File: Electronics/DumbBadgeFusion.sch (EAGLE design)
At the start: 103 parts, among them IC1 SN74CBT16233DGGR, IC2 SN74CBT16233DGGR, SW1 SPST_TACT-KMR2, U1 TDP3E001DRLR-SOT-23-5SOT-23-5, U6 MAX3232, U7 TPS61090RSAR, U8 MCP73831T-2ACI/OT, X4 32.768

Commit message: beginning Firmware
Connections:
- new net LCD0: U$4.PB00
- new net LCD1: U$4.PB01
- new net LCD10: U$4.PB10
- new net LCD11: U$4.PB11
- new net LCD12: U$4.PB12
- new net LCD13: U$4.PB13
- new net LCD14: U$4.PB14
- new net LCD15: U$4.PB15
- new net LCD2: U$4.PB02
- new net LCD3: U$4.PB03
- new net LCD4: U$4.PB04
- new net LCD5: U$4.PB05
- new net LCD6: U$4.PB06
- new net LCD7: U$4.PB07
- new net LCD8: U$4.PB08
- new net LCD9: U$4.PB09
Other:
- moved on the sheet: U$4
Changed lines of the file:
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@@
 <attribute name="SHEET" x="363.22" y="-0.635" size="2.54" layer="94" font="vector"/>
 </instance>
-<instance part="U$4" gate="G$1" x="152.4" y="78.74" smashed="yes">
-<attribute name="NAME" x="137.16" y="12.7" size="1.778" layer="95"/>
-<attribute name="VALUE" x="137.16" y="104.648" size="1.778" layer="96"/>
+<instance part="U$4" gate="G$1" x="175.26" y="81.28" smashed="yes">
+<attribute name="NAME" x="160.02" y="15.24" size="1.778" layer="95"/>
+<attribute name="VALUE" x="160.02" y="107.188" size="1.778" layer="96"/>
 </instance>
 <instance part="IC1" gate="G$1" x="248.92" y="226.06" smashed="yes">
@@
 </instances>
 <busses>
+<bus name="LCD[0..15]">
+<segment>
+<wire x1="134.62" y1="81.28" x2="134.62" y2="43.18" width="0.762" layer="92"/>
+<label x="133.35" y="58.928" size="1.778" layer="95" rot="R90"/>
+</segment>
+</bus>
 </busses>
 <nets>
@@
 </segment>
 </net>
+<net name="LCD0" class="0">
+<segment>
+<wire x1="134.62" y1="81.28" x2="142.24" y2="81.28" width="0.1524" layer="91"/>
+<wire x1="142.24" y1="81.28" x2="154.94" y2="81.28" width="0.1524" layer="91"/>
+<label x="144.78" y="81.28" size="1.778" layer="95"/>
+<pinref part="U$4" gate="G$1" pin="PB00"/>
+</segment>
+</net>
+<net name="LCD1" class="0">
+<segment>
+<wire x1="134.62" y1="78.74" x2="142.24" y2="78.74" width="0.1524" layer="91"/>
+<wire x1="142.24" y1="78.74" x2="154.94" y2="78.74" width="0.1524" layer="91"/>
+<label x="144.78" y="78.74" size="1.778" layer="95"/>
+<pinref part="U$4" gate="G$1" pin="PB01"/>
+</segment>
+</net>
+<net name="LCD2" class="0">
+<segment>
+<wire x1="134.62" y1="76.2" x2="142.24" y2="76.2" width="0.1524" layer="91"/>
+<wire x1="142.24" y1="76.2" x2="154.94" y2="76.2" width="0.1524" layer="91"/>
+<label x="144.78" y="76.2" size="1.778" layer="95"/>
+<pinref part="U$4" gate="G$1" pin="PB02"/>
+</segment>
+</net>
+<net name="LCD3" class="0">
+<segment>
+<wire x1="134.62" y1="73.66" x2="142.24" y2="73.66" width="0.1524" layer="91"/>
+<wire x1="142.24" y1="73.66" x2="154.94" y2="73.66" width="0.1524" layer="91"/>
+<label x="144.78" y="73.66" size="1.778" layer="95"/>
+<pinref part="U$4" gate="G$1" pin="PB03"/>
+</segment>
+</net>
+<net name="LCD4" class="0">
+<segment>
+<wire x1="134.62" y1="71.12" x2="142.24" y2="71.12" width="0.1524" layer="91"/>
+<wire x1="142.24" y1="71.12" x2="154.94" y2="71.12" width="0.1524" layer="91"/>
+<label x="144.78" y="71.12" size="1.778" layer="95"/>
+<pinref part="U$4" gate="G$1" pin="PB04"/>
+</segment>
+</net>
+<net name="LCD5" class="0">
+<segment>
+<wire x1="134.62" y1="68.58" x2="142.24" y2="68.58" width="0.1524" layer="91"/>
+<wire x1="142.24" y1="68.58" x2="154.94" y2="68.58" width="0.1524" layer="91"/>
+<label x="144.78" y="68.58" size="1.778" layer="95"/>
+<pinref part="U$4" gate="G$1" pin="PB05"/>
+</segment>
+</net>
+<net name="LCD6" class="0">
+<segment>
+<wire x1="134.62" y1="66.04" x2="142.24" y2="66.04" width="0.1524" layer="91"/>
+<wire x1="142.24" y1="66.04" x2="154.94" y2="66.04" width="0.1524" layer="91"/>
+<label x="144.78" y="66.04" size="1.778" layer="95"/>
+<pinref part="U$4" gate="G$1" pin="PB06"/>
+</segment>
+</net>
+<net name="LCD7" class="0">
+<segment>
+<wire x1="134.62" y1="63.5" x2="142.24" y2="63.5" width="0.1524" layer="91"/>
+<wire x1="142.24" y1="63.5" x2="154.94" y2="63.5" width="0.1524" layer="91"/>
+<label x="144.78" y="63.5" size="1.778" layer="95"/>
+<pinref part="U$4" gate="G$1" pin="PB07"/>
+</segment>
+</net>
+<net name="LCD8" class="0">
+<segment>
+<wire x1="134.62" y1="60.96" x2="142.24" y2="60.96" width="0.1524" layer="91"/>
+<wire x1="142.24" y1="60.96" x2="154.94" y2="60.96" width="0.1524" layer="91"/>
+<label x="144.78" y="60.96" size="1.778" layer="95"/>
+<pinref part="U$4" gate="G$1" pin="PB08"/>
+</segment>
+</net>
+<net name="LCD9" class="0">
+<segment>
+<wire x1="134.62" y1="58.42" x2="142.24" y2="58.42" width="0.1524" layer="91"/>
+<wire x1="142.24" y1="58.42" x2="154.94" y2="58.42" width="0.1524" layer="91"/>
+<label x="144.78" y="58.42" size="1.778" layer="95"/>
+<pinref part="U$4" gate="G$1" pin="PB09"/>
+</segment>
+</net>
+<net name="LCD10" class="0">
+<segment>
+<wire x1="134.62" y1="55.88" x2="142.24" y2="55.88" width="0.1524" layer="91"/>
+<wire x1="142.24" y1="55.88" x2="154.94" y2="55.88" width="0.1524" layer="91"/>
+<label x="144.78" y="55.88" size="1.778" layer="95"/>
+<pinref part="U$4" gate="G$1" pin="PB10"/>
+</segment>
+</net>
+<net name="LCD11" class="0">
+<segment>
+<wire x1="134.62" y1="53.34" x2="142.24" y2="53.34" width="0.1524" layer="91"/>
+<wire x1="142.24" y1="53.34" x2="154.94" y2="53.34" width="0.1524" layer="91"/>
+<label x="144.78" y="53.34" size="1.778" layer="95"/>
+<pinref part="U$4" gate="G$1" pin="PB11"/>
+</segment>
+</net>
+<net name="LCD12" class="0">
+<segment>
+<wire x1="134.62" y1="50.8" x2="142.24" y2="50.8" width="0.1524" layer="91"/>
+<wire x1="142.24" y1="50.8" x2="154.94" y2="50.8" width="0.1524" layer="91"/>
+<label x="144.78" y="50.8" size="1.778" layer="95"/>
+<pinref part="U$4" gate="G$1" pin="PB12"/>
+</segment>
+</net>
+<net name="LCD13" class="0">
+<segment>
+<wire x1="134.62" y1="48.26" x2="142.24" y2="48.26" width="0.1524" layer="91"/>
+<wire x1="142.24" y1="48.26" x2="154.94" y2="48.26" width="0.1524" layer="91"/>
+<label x="144.78" y="48.26" size="1.778" layer="95"/>
+<pinref part="U$4" gate="G$1" pin="PB13"/>
+</segment>
+</net>
+<net name="LCD14" class="0">
+<segment>
+<wire x1="134.62" y1="45.72" x2="142.24" y2="45.72" width="0.1524" layer="91"/>
+<wire x1="142.24" y1="45.72" x2="154.94" y2="45.72" width="0.1524" layer="91"/>
+<label x="144.78" y="45.72" size="1.778" layer="95"/>
+<pinref part="U$4" gate="G$1" pin="PB14"/>
+</segment>
+</net>
+<net name="LCD15" class="0">
+<segment>
+<wire x1="134.62" y1="43.18" x2="142.24" y2="43.18" width="0.1524" layer="91"/>
+<wire x1="142.24" y1="43.18" x2="154.94" y2="43.18" width="0.1524" layer="91"/>
+<label x="144.78" y="43.18" size="1.778" layer="95"/>
+<pinref part="U$4" gate="G$1" pin="PB15"/>
+</segment>
+</net>

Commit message: power supply
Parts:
- removed B1: S2B-PH-SM4-TB(LF)(SN), microbuilder:BATTERY
- removed C29: 100uF/6V, microbuilder:CAP_TANTALUMB/3528_REFLOW
- removed C30: 10µF, microbuilder:CAP_CERAMIC0805-NOOUTLINE
- removed L2: VLC5045-6.8uH, microbuilder:INDUCTORTDK_VLC5045
- removed R1: 340k, microbuilder:RESISTOR0805_NOOUTLINE
- removed R79, R82: 1.87Mohm, microbuilder:RESISTOR0805_NOOUTLINE
- removed R80: 200K, microbuilder:RESISTOR0805_NOOUTLINE
- removed R81: 340K, microbuilder:RESISTOR0805_NOOUTLINE
- removed R86: 2k, microbuilder:RESISTOR0805_NOOUTLINE
- removed U7: TPS61090RSAR, microbuilder:VREG_TPS6103X
- removed U8: MCP73831T-2ACI/OT, microbuilder:MCP73831/2
- added B2: JST 2-PH, microbuilder:BATTERY
- added C2, C7: 10uF, microbuilder:CAP_CERAMIC0805-NOOUTLINE
- added C3: 2.2uF, microbuilder:CAP_CERAMIC0805-NOOUTLINE
- added C4: 0.1uF, microbuilder:CAP_CERAMIC0805_10MGAP
- added C6: 100uF, rcl:C-USC1210
- added CHRG/LBO: ORANGE, microbuilder:LED0805_NOOUTLINE
- added DONE: GREEN, microbuilder:LED0805_NOOUTLINE
- added FID1, FID2, FID3: FIDUCIAL"", microbuilder:FIDUCIAL""
- added JP2: (no value), microbuilder:HEADER-1X8ROUND
- added L1: 6.8uH, microbuilder:INDUCTORTDK_VLC5045
- added LED1: RED, microbuilder:LED0805_NOOUTLINE
- added LED2: BLUE, microbuilder:LED0805_NOOUTLINE
- added R10, R17: 100K, microbuilder:RESISTOR0805_NOOUTLINE
- added R11, R14, R20, R5: 1K, microbuilder:RESISTOR0805_NOOUTLINE
- added R13, R6: 200K, microbuilder:RESISTOR0805_NOOUTLINE
- added R16: 1.0K, microbuilder:RESISTOR0805_NOOUTLINE
- added R4: 1.87M, microbuilder:RESISTOR0805_NOOUTLINE
- added R7: 340K, microbuilder:RESISTOR_0805MP
- added R8: 1.87M, microbuilder:RESISTOR_0805MP
- added R9: 270K, microbuilder:RESISTOR0805_NOOUTLINE
- added T1: MMUN2133LT1G, transistor:MUN2114T1-PNP_DRIVER-SC59-BEC
- added THERM: 15K, microbuilder:RESISTOR0805_NOOUTLINE
- added U$12, U$13: MOUNTINGHOLE2.5, microbuilder:MOUNTINGHOLE2.5
- added U2: TPS61090RSAR, microbuilder:VREG_TPS6103X
- added U3: MCP73871, microbuilder:MCP73871
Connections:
- removed net N$73: L2.2, U7.SW
- removed net N$74: R81.2, R82.1, U7.LBI
- removed net N$76: R79.1, R80.2, U7.FB
- removed net N$81: R86.1, U8.PROG
- removed net VDD1: C30.1, U8.VDD
- removed net VUSB: C1.1, U1.5, USB.VBUS
- new net LBO: JP2.6, T1.B, U2.LBO
- new net N$10: R10.1, R9.1, U3.VPCC
- new net N$11: R14.1, U3.STAT2
- new net N$13: R11.1, U3.STAT1/LBO
- new net N$14: THERM.2, U3.THERM
- new net N$16: R16.2, U3.PROG1
- new net N$17: DONE.C, R14.2
- new net N$18: CHRG/LBO.C, R11.2
- new net N$19: R17.2, U3.PROG3
- new net N$2: L1.2, U2.SW
- new net N$4: R7.2, R8.1, U2.LBI
- new net N$5: LED1.A, R20.1
- new net N$7: R4.1, R6.2, U2.FB
- new net N$8: R20.2, T1.C
- new net N$9: LED2.A, R5.2
- new net VBUS: C1.1, CHRG/LBO.A, DONE.A, JP2.1, R9.2, U1.5, U3./TE, U3.CE, U3.PROG2, U3.SEL, U3.VIN1, U3.VIN2, USB.VBUS
- new net VLIPO: B2.+, C7.1, JP2.2, U3.VBAT1, U3.VBAT2, U3.VBATSENS
- net 5.0V: now also C3.1, C6.1, JP2.8, R4.2, R5.1, U2.VOUT; no longer C29.+, R79.2, U7.VOUT
- net ENABLE: now also JP2.4, R13.2, U2.EN; no longer R1.1, U7.EN
- net GND: now also B2.-, C2.2, C3.2, C4.2, C6.2, C7.2, JP2.5, JP2.7, LED1.C, LED2.C, R10.2, R16.1, R17.1, R6.1, R7.1, THERM.1, U2.GND, U2.PGND, U2.SYNC, U3.THERMAL, U3.VSS1, U3.VSS2; no longer B1.-, C29.-, C30.2, R80.1, R81.1, R86.2, U7.GND, U7.PGND, U7.SYNC, U8.VSS
- net VBAT: now also C2.1, C4.1, JP2.3, L1.1, R13.1, R8.2, T1.E, U2.VBAT, U3.VOUT1, U3.VOUT2; no longer B1.+, L2.1, R1.2, R82.2, U7.VBAT, U8.VBAT
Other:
- note added: "1.0K = 1000mA"
- note added: "10K NTC Thermistor:"
- note added: "Charge Rate = 1000V/PROG1"
- note added: "No Thermistor:"
- note added: "On/Off Switch"
- note added: "R3 = 1.9Mohm for 5.2V R3 = 1.1Mohm for 3.3V"
- note added: "RT1 = 0, RT2 = 10K"
- note added: "RT1 = TBD, RT2 = TBD"
- note removed: "R2 < 500K R1 = 5.5*R2 (3.2V LBO)"
- note removed: "R4 = 200K R3 = 1.85Mohm"
- note removed: "With apologies to Adafruit The power circuit is a rip-off of the PowerBoost 500C"

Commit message: more power
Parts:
- removed JP2: (no value), microbuilder:HEADER-1X8ROUND
- added C5: 100uF, rcl:C-USC1210
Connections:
- net 3V3: now also C5.1
- net 5.0V: no longer JP2.8
- net ENABLE: no longer JP2.4
- net GND: now also C5.2; no longer JP2.5, JP2.7
- net LBO: no longer JP2.6
- net VBAT: no longer JP2.3
- net VBUS: no longer JP2.1
- net VLIPO: no longer JP2.2
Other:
- note added: "3.3 V Reg"
- note added: "5 V Switching Reg"
- note added: "Battery Charging"
- note added: "Power Sw"
- note removed: "On/Off Switch"
- note removed: "R3 = 1.9Mohm for 5.2V R3 = 1.1Mohm for 3.3V"
- moved on the sheet: R13

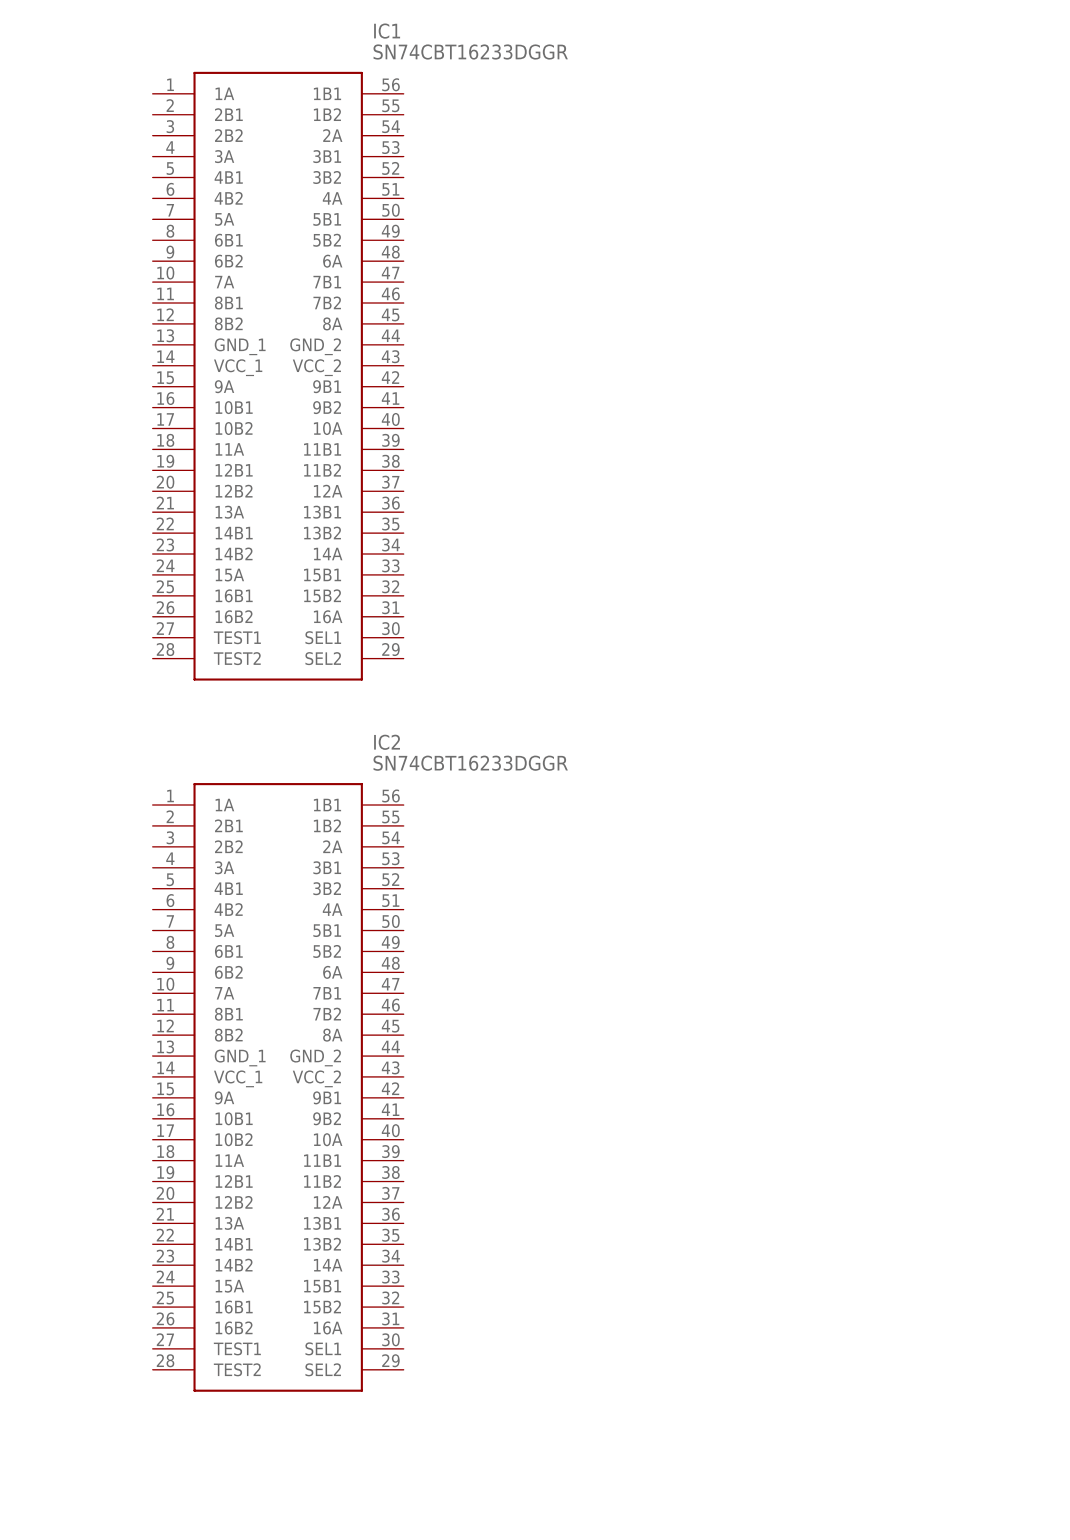
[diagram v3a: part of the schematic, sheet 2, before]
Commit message: added FPC conn
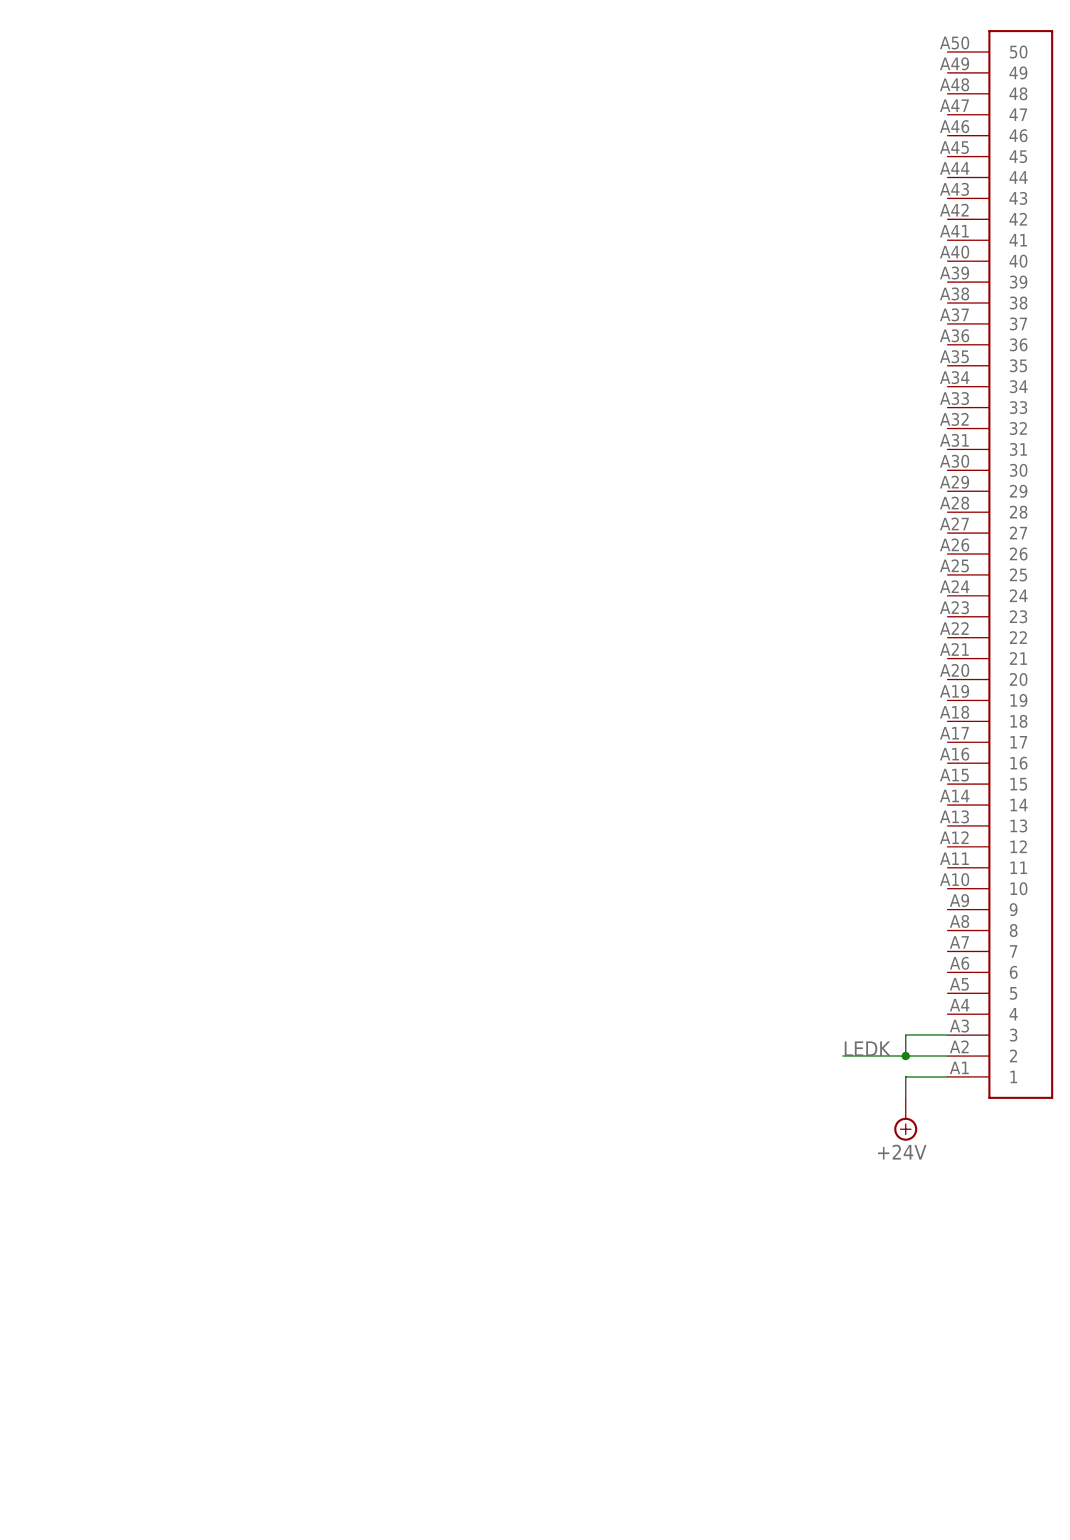
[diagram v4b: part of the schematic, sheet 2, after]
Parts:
- removed IC1, IC2: SN74CBT16233DGGR, SamacSys_Parts:SN74CBT16233DGGR
- added C10, C11: 1uF, SparkFun-Capacitors:0.1UF-0603-25V-(+80/-20%)
- added C8: 10uF, SparkFun-Capacitors:0.1UF-0603-25V-(+80/-20%)
- added C9: 0.1uF, SparkFun-Capacitors:0.1UF-0603-25V-(+80/-20%)
- added D1: MM3Z24VT1G, microbuilder:DIODESMA
- added D2: MBR0540, microbuilder:DIODESOD-123
- added L2: 6.8uH power L CID 2276, microbuilder:INDUCTORNR5040
- added R1: 10k, adafruit:R-US_R0603
- added R12: 6, adafruit:R-US_R0603
- added U$30: 50PINFPC, FPC:50PINFPC
- added U4: FAN5333BSX, microbuilder:FAN5331
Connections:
- new net +24V: C10.1, C11.1, D1.C, D2.C, U$30.1
- new net LEDK: C9.1, D1.A, R12.2, U$30.2, U$30.3, U4.FB
- new net N$20: D2.A, L2.2, U4.SW
- new net N$21: C8.1, L2.1, R1.2, U4.VIN
- new net PWM: R1.1, U4.SHDN
- net GND: now also C10.2, C11.2, C8.2, C9.2, R12.1, U4.GND
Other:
- note added: "24 V Boost"
- note added: "7 x 3.2V LED boost"

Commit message: updated something
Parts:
- added IC1, IC2, IC3: 74245MTC, adafruit:74245MTC
- added U$32: RPI-ZERO, RPI-Zero:RPI-ZERO
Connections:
- new net CS: IC3A.B5, U$30.42
- new net D/C: IC3A.B6, U$30.41
- new net DB00: IC2A.B8, U$30.13
- new net DB01: IC2A.B7, U$30.14
- new net DB02: IC2A.B6, U$30.15
- new net DB03: IC2A.B5, U$30.16
- new net DB04: IC2A.B4, U$30.17
- new net DB05: IC2A.B3, U$30.18
- new net DB06: IC2A.B2, U$30.19
- new net DB07: IC2A.B1, U$30.20
- new net DB08: IC1A.B8, U$30.21
- new net DB09: IC1A.B7, U$30.22
- new net DB10: IC1A.B6, U$30.23
- new net DB11: IC1A.B5, U$30.24
- new net DB12: IC1A.B4, U$30.25
- new net DB13: IC1A.B3, U$30.26
- new net DB14: IC1A.B2, U$30.27
- new net DB15: IC1A.B1, U$30.28
- new net DE: U$30.12
- new net DOTCLK: U$30.11
- new net LCDRST: IC3A.B4, U$30.8
- new net LCD_CS: IC3A.A5, U$4.PB22
- new net LCD_D/C: IC3A.A6, U$4.PB23
- new net LCD_RD: IC1A.DIR, IC2A.DIR, IC3A.A8, IC3A.DIR, U$4.PB16
- new net LCD_RESET: IC3A.A4, U$4.PB30
- new net LCD_W/R: IC3A.A7, U$4.PB17
- new net RD: IC3A.B8, U$30.39
- new net SDO: U$30.37
- new net WR: IC3A.B7, U$30.40
- new net XL/INT: U$30.48
- new net XR/SCL: U$30.46
- new net YD/SDA: U$30.47
- new net YU/RES: U$30.49
- net 3V3: now also U$30.4, U$30.43, U$30.44
- net 5.0V: now also U$32.5V0@1, U$32.5V0@2
- net GND: now also IC1A.G, IC2A.G, IC3A.G, U$30.10, U$30.29, U$30.30, U$30.31, U$30.32, U$30.33, U$30.34, U$30.35, U$30.36, U$30.38, U$30.45, U$30.5, U$30.50, U$30.6, U$30.7, U$30.9, U$32.GND@1, U$32.GND@2, U$32.GND@3, U$32.GND@4, U$32.GND@5, U$32.GND@6, U$32.GND@7, U$32.GND@8
- net LCD0: now also IC2A.A8
- net LCD1: now also IC2A.A7
- net LCD10: now also IC1A.A6
- net LCD11: now also IC1A.A5
- net LCD12: now also IC1A.A4
- net LCD13: now also IC1A.A3
- net LCD14: now also IC1A.A2
- net LCD15: now also IC1A.A1
- net LCD2: now also IC2A.A6
- net LCD3: now also IC2A.A5
- net LCD4: now also IC2A.A4
- net LCD5: now also IC2A.A3
- net LCD6: now also IC2A.A2
- net LCD7: now also IC2A.A1
- net LCD8: now also IC1A.A8
- net LCD9: now also IC1A.A7
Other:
- moved on the sheet: C22, C23, C24, C26, C27, C28, SW1, TP3, TP4, U$4, U6, X4

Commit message: fixing power supply
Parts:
- removed FID1, FID2, FID3: FIDUCIAL"", microbuilder:FIDUCIAL""
- removed THERM: 15K, microbuilder:RESISTOR0805_NOOUTLINE
- removed U$12, U$13: MOUNTINGHOLE2.5, microbuilder:MOUNTINGHOLE2.5
- added NCP21XW153J03RA: 15K, microbuilder:RESISTOR0805_NOOUTLINE
- added TP1, TP2, TP5, TP6, TP7, TP8: TPB1,27, testpad:TPB1,27
- TP3, TP4: value (none) -> TPB1,27; device microbuilder:TESTPOINTROUND1.5MM -> testpad:TPB1,27
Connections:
- removed net SWCLK: TP3.P$1
- removed net SWDIO: TP4.P$1
- net +24V: now also TP7.TP
- net 3V3: now also TP6.TP
- net 5.0V: now also TP5.TP
- net GND: now also NCP21XW153J03RA.1, TP4.TP; no longer THERM.1
- net LEDK: now also TP8.TP
- net N$14: now also NCP21XW153J03RA.2; no longer THERM.2
- net USB_N: now also U$4.PA24/I12/SERCOM3+5.2/D-
- net USB_P: now also U$4.PA25/I13/SERCOM3+5.3/D+
- net VBAT: now also TP2.TP
- net VBUS: now also TP1.TP
- net VLIPO: now also TP3.TP
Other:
- note added: "1.8 V Reg"
- note removed: "Power Sw"
